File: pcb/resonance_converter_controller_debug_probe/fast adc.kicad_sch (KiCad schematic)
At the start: 42 parts, among them U13 THS4541IRGTT, U14 OPA333xxDBV, U15 THS4541IRGTT, U16 MCP4441-xxxx-ST, U7 ADC3910D125IRSMT, U8 OPA333xxDBV

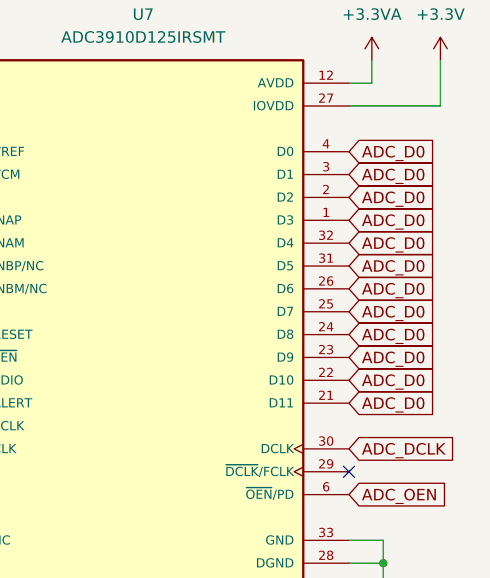
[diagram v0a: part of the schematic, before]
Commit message: Add schematic for debug probe
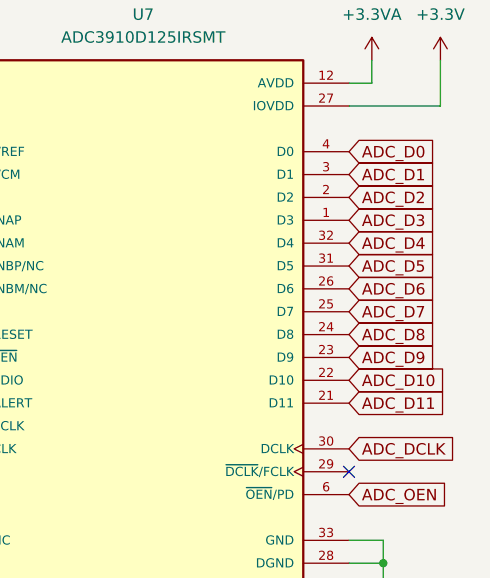
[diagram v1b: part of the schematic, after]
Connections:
- net ADC_D0: no longer U7.1 (D3), U7.2 (D2), U7.21 (D11), U7.22 (D10), U7.23 (D9), U7.24 (D8), U7.25 (D7), U7.26 (D6), U7.3 (D1), U7.31 (D5), U7.32 (D4)
- new net ADC_D1: U7.3 (D1)
- new net ADC_D10: U7.22 (D10)
- new net ADC_D11: U7.21 (D11)
- new net ADC_D2: U7.2 (D2)
- new net ADC_D3: U7.1 (D3)
- new net ADC_D4: U7.32 (D4)
- new net ADC_D5: U7.31 (D5)
- new net ADC_D6: U7.26 (D6)
- new net ADC_D7: U7.25 (D7)
- new net ADC_D8: U7.24 (D8)
- new net ADC_D9: U7.23 (D9)

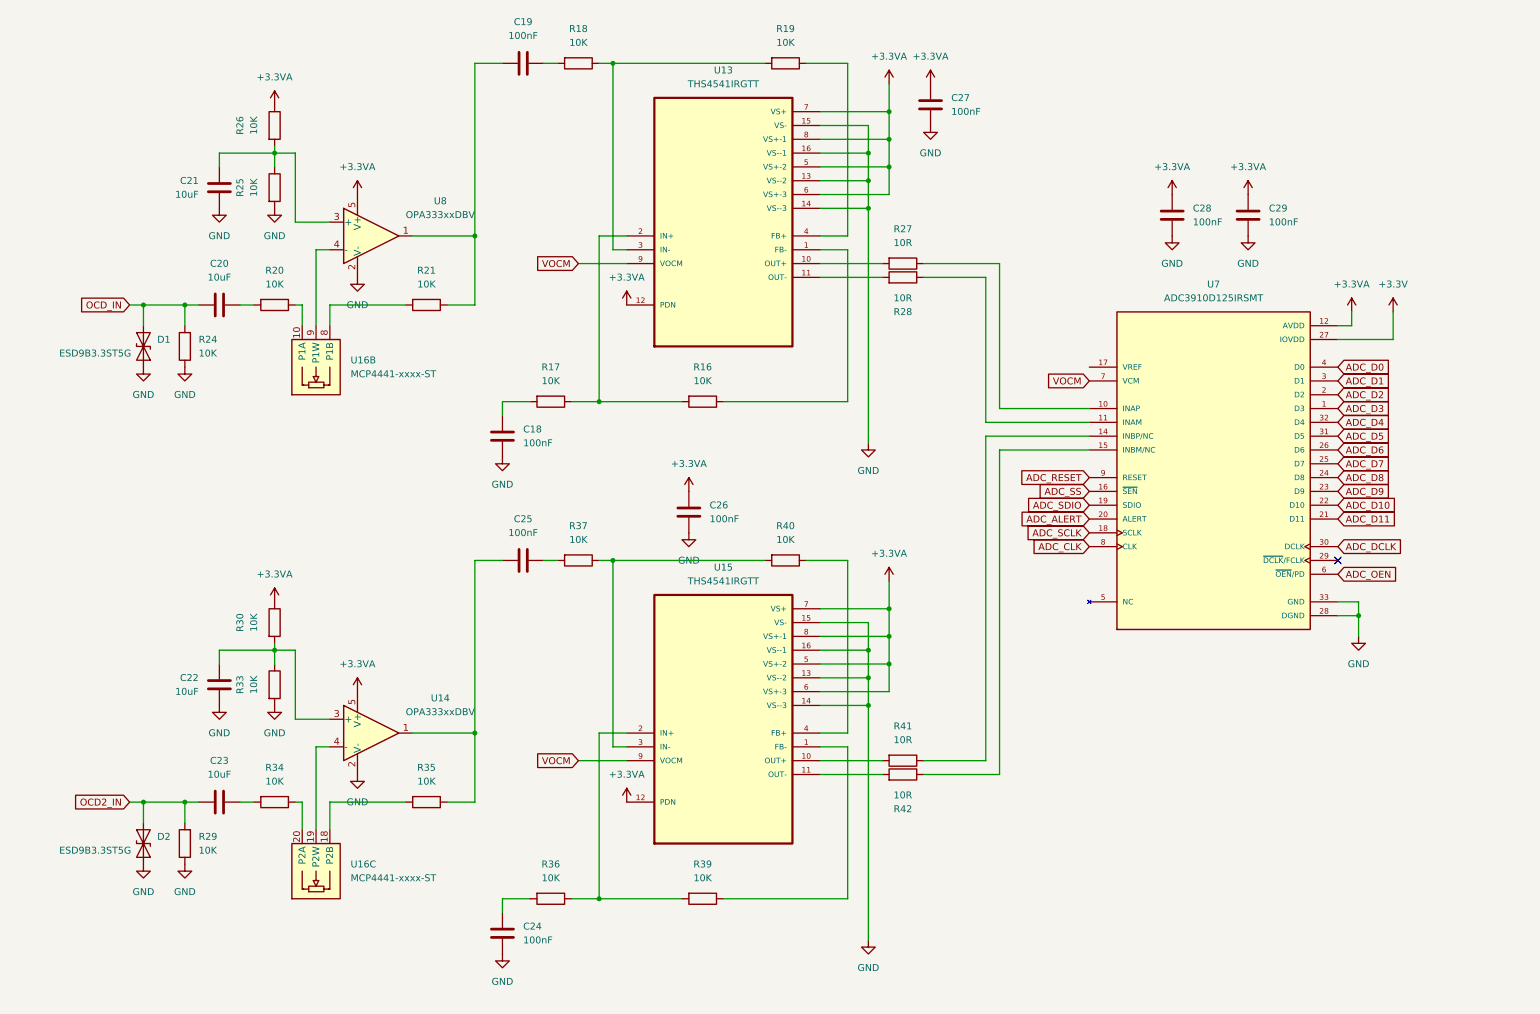
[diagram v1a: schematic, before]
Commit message: Fix schematic and initial component layout
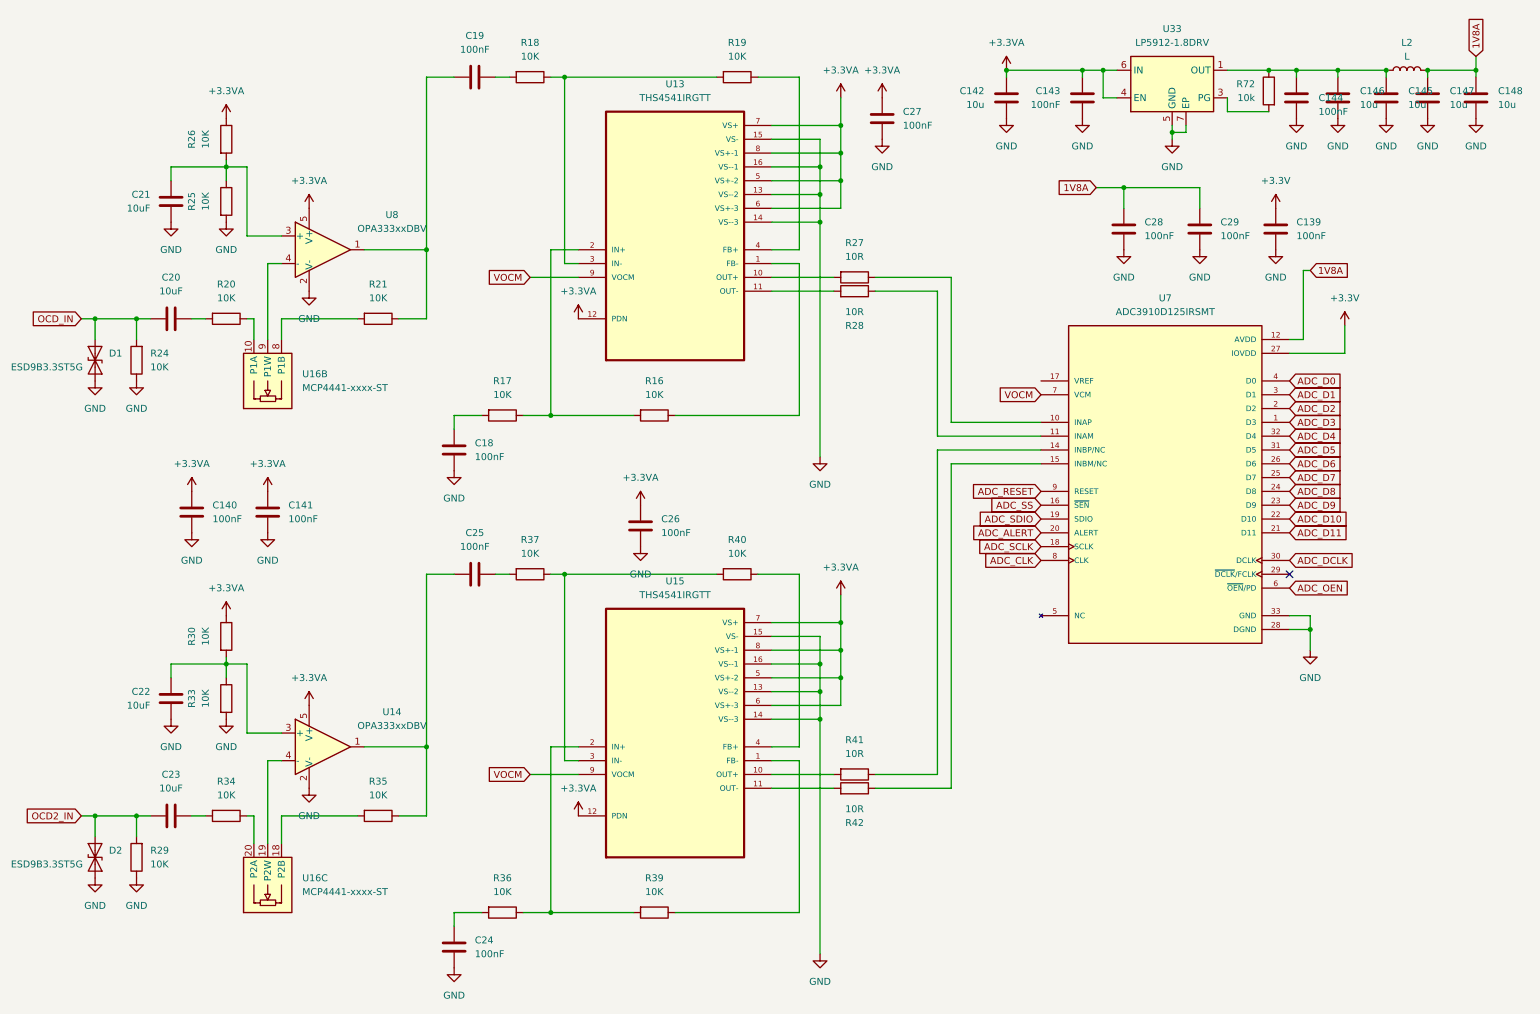
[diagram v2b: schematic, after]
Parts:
- added C139, C140, C141, C143, C144: 100nF, Capacitor_SMD:C_0402_1005Metric, symbol Device:C
- added C142, C145, C146, C147, C148: 10u, Capacitor_SMD:C_0805_2012Metric, symbol Device:C
- added L2: L, Inductor_SMD:L_0805_2012Metric, symbol Device:L
- added R72: 10k, Resistor_SMD:R_0402_1005Metric, symbol Device:R
- added U33: LP5912-1.8DRV, Package_SON:WSON-6-1EP_2x2mm_P0.65mm_EP1x1.6mm_ThermalVias, symbol Regulator_Linear:LP5912-1.8DRV
- U16: footprint Package_SO:TSSOP-20_4.4x6.5mm_P0.65mm -> Package_DFN_QFN:Texas_RGP0020H_VQFN-20-1EP_4x4mm_P0.5mm_EP2.4x2.4mm_ThermalVias
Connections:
- net +3.3V: now also C139.1
- net +3.3VA: now also C140.1, C141.1, C142.1, C143.1, U33.4 (EN), U33.6 (IN); no longer C28.1, C29.1, U7.12 (AVDD), U7.13 (AVDD)
- net GND: now also C139.2, C140.2, C141.2, C142.2, C143.2, C144.2, C145.2, C146.2, C147.2, C148.2, U33.5 (GND), U33.7 (EP)
- new net: C144.1, C145.1, C146.1, L2.1, R72.1, U33.1 (OUT)
- new net: R72.2, U33.3 (PG)
- new net AVDD: C147.1, C148.1, C28.1, C29.1, L2.2, U7.12 (AVDD), U7.13 (AVDD)
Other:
- moved on the sheet: C18, C19, C20, C21, C22, C23, C24, C25, C26, C27, C28, C29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
